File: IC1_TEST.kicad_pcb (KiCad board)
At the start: 4 copper layers, 26 parts, among them IC1 ADM3054WBRWZ-RL7-!my_lib, J1 B4B-XH-A_LF__SN_-!my_lib, SW1 SW_DIP_x03, SW2 SW_Push, U1 DEV-16771, U2 MAX6369KA+T

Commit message: wiring changes
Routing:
- net DIO_BUTTON: track 62.9 -> 58.9 mm
- net DIO_WATCHDOG: track 92.9 -> 89.5 mm
- net LED1: track 94.1 -> 97.0 mm
- net 3.3v_SUPPLY: track 246.1 -> 248.0 mm
- net SET2: track 18.3 -> 20.1 mm
- net SET1: track 37.8 -> 39.0 mm
- net LED2: track 70.0 -> 69.0 mm
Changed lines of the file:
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@@
     )
   )
-  (segment (start 195.633564 87.775489) (end 204.216 85.852) (width 0.25) (layer "F.Cu") (net 1))
-  (segment (start 206.756 116.84) (end 185.839295 135.89) (width 0.25) (layer "F.Cu") (net 1))
-  (segment (start 204.216 85.852) (end 206.756 85.852) (width 0.25) (layer "F.Cu") (net 1))
-  (segment (start 206.756 85.852) (end 206.756 116.84) (width 0.25) (layer "F.Cu") (net 1))
-  (segment (start 189.134052 94.275001) (end 195.633564 87.775489) (width 0.25) (layer "F.Cu") (net 1))
+  (segment (start 189.134052 94.275001) (end 195.58 87.376) (width 0.25) (layer "F.Cu") (net 1))
+  (segment (start 205.232 117.324273) (end 185.839295 135.89) (width 0.25) (layer "F.Cu") (net 1))
+  (segment (start 205.232 86.868) (end 205.232 117.324273) (width 0.25) (layer "F.Cu") (net 1))
   (segment (start 185.839295 135.89) (end 172.72 135.89) (width 0.25) (layer "F.Cu") (net 1))
+  (segment (start 195.58 87.376) (end 205.232 86.868) (width 0.25) (layer "F.Cu") (net 1))
   (segment (start 135.0137 142.875) (end 136.525 142.875) (width 0.25) (layer "F.Cu") (net 2))
   (segment (start 135.0137 149.225) (end 137.863402 149.225) (width 0.25) (layer "F.Cu") (net 2))
@@
   (segment (start 185.674 109.22) (end 185.674 96.266) (width 0.25) (layer "In1.Cu") (net 4))
   (segment (start 185.674 96.266) (end 185.928 96.012) (width 0.25) (layer "In1.Cu") (net 4))
-  (segment (start 191.865948 96.224999) (end 198.415001 96.224999) (width 0.25) (layer "F.Cu") (net 5))
-  (segment (start 198.415001 96.224999) (end 203.2 91.44) (width 0.25) (layer "F.Cu") (net 5))
+  (segment (start 203.2 91.44) (end 199.136 97.028) (width 0.25) (layer "F.Cu") (net 5))
+  (segment (start 199.136 97.028) (end 192.668949 97.028) (width 0.25) (layer "F.Cu") (net 5))
+  (segment (start 192.668949 97.028) (end 191.865948 96.224999) (width 0.25) (layer "F.Cu") (net 5))
   (segment (start 223.52 101.6) (end 217.894511 95.974511) (width 0.25) (layer "B.Cu") (net 5))
   (segment (start 205.74 91.44) (end 203.2 91.44) (width 0.25) (layer "B.Cu") (net 5))
   (segment (start 217.894511 95.974511) (end 210.274511 95.974511) (width 0.25) (layer "B.Cu") (net 5))
   (segment (start 210.274511 95.974511) (end 205.74 91.44) (width 0.25) (layer "B.Cu") (net 5))
+  (segment (start 195.072 96.52) (end 198.628 96.52) (width 0.25) (layer "F.Cu") (net 6))
   (segment (start 203.2 93.98) (end 203.2 100.33) (width 0.25) (layer "F.Cu") (net 6))
-  (segment (start 197.832948 95.575001) (end 198.882449 94.5255) (width 0.25) (layer "F.Cu") (net 6))
-  (segment (start 191.865948 95.575001) (end 197.832948 95.575001) (width 0.25) (layer "F.Cu") (net 6))
+  (segment (start 194.127001 95.575001) (end 191.865948 95.575001) (width 0.25) (layer "F.Cu") (net 6))
+  (segment (start 195.072 96.52) (end 194.127001 95.575001) (width 0.25) (layer "F.Cu") (net 6))
+  (segment (start 198.628 96.52) (end 198.882449 94.5255) (width 0.25) (layer "F.Cu") (net 6))
   (via (at 198.882449 94.5255) (size 0.8) (drill 0.4) (layers "F.Cu" "B.Cu") (net 6))
   (segment (start 198.882449 94.5255) (end 199.427949 93.98) (width 0.25) (layer "In2.Cu") (net 6))
@@
   (segment (start 196.85 94.850501) (end 196.2745 94.275001) (width 0.25) (layer "F.Cu") (net 8))
   (segment (start 118.872 147.828) (end 118.872 128.016) (width 0.25) (layer "F.Cu") (net 8))
-  (segment (start 190.5 96.234419) (end 189.969009 96.76541) (width 0.25) (layer "F.Cu") (net 8))
   (segment (start 140.938911 144.811089) (end 137.795 147.955) (width 0.25) (layer "F.Cu") (net 8))
   (segment (start 157.48 151.13) (end 151.161089 144.811089) (width 0.25) (layer "F.Cu") (net 8))
+  (segment (start 180.705 97.536) (end 177.95 93.4) (width 0.25) (layer "F.Cu") (net 8))
   (segment (start 142.12 93.4) (end 171.45 93.4) (width 0.25) (layer "F.Cu") (net 8))
   (segment (start 137.795 147.955) (end 135.0137 147.955) (width 0.25) (layer "F.Cu") (net 8))
-  (segment (start 191.865948 94.275001) (end 191.161374 94.275001) (width 0.25) (layer "F.Cu") (net 8))
   (segment (start 135.0137 147.955) (end 131.1247 147.955) (width 0.25) (layer "F.Cu") (net 8))
-  (segment (start 189.969009 96.76541) (end 181.31541 96.76541) (width 0.25) (layer "F.Cu") (net 8))
+  (segment (start 190.5 94.936375) (end 190.5 97.536) (width 0.25) (layer "F.Cu") (net 8))
   (segment (start 137.77 89.05) (end 142.12 93.4) (width 0.25) (layer "F.Cu") (net 8))
-  (segment (start 191.161374 94.275001) (end 190.5 94.936375) (width 0.25) (layer "F.Cu") (net 8))
   (segment (start 196.2745 94.275001) (end 191.865948 94.275001) (width 0.25) (layer "F.Cu") (net 8))
   (segment (start 151.161089 144.811089) (end 140.938911 144.811089) (width 0.25) (layer "F.Cu") (net 8))
+  (segment (start 190.5 97.536) (end 180.705 97.536) (width 0.25) (layer "F.Cu") (net 8))
+  (segment (start 191.865948 94.275001) (end 191.161374 94.275001) (width 0.25) (layer "F.Cu") (net 8))
   (segment (start 215.900001 158.75) (end 215.9 123.444) (width 0.25) (layer "F.Cu") (net 8))
-  (segment (start 181.31541 96.76541) (end 177.95 93.4) (width 0.25) (layer "F.Cu") (net 8))
-  (segment (start 190.5 94.936375) (end 190.5 96.234419) (width 0.25) (layer "F.Cu") (net 8))
+  (segment (start 191.161374 94.275001) (end 190.5 94.936375) (width 0.25) (layer "F.Cu") (net 8))
   (segment (start 215.9 123.444) (end 207.659011 95.25) (width 0.25) (layer "F.Cu") (net 8))
   (segment (start 118.872 128.016) (end 137.77 89.05) (width 0.25) (layer "F.Cu") (net 8))
@@
   (segment (start 161.036 159.512) (end 172.72 153.67) (width 0.25) (layer "B.Cu") (net 16))
   (segment (start 149.86 123.952) (end 149.86 159.512) (width 0.25) (layer "B.Cu") (net 16))
+  (segment (start 112.776 150.368) (end 112.776 169.164) (width 0.25) (layer "In1.Cu") (net 17))
+  (segment (start 112.92 139.7) (end 112.776 150.368) (width 0.25) (layer "In1.Cu") (net 17))
+  (segment (start 112.776 169.164) (end 154.94 169.164) (width 0.25) (layer "In1.Cu") (net 17))
   (segment (start 154.94 169.164) (end 172.72 151.13) (width 0.25) (layer "In1.Cu") (net 17))
-  (segment (start 115.824 169.164) (end 154.94 169.164) (width 0.25) (layer "In1.Cu") (net 17))
-  (segment (start 113.792 151.384) (end 115.824 169.164) (width 0.25) (layer "In1.Cu") (net 17))
-  (segment (start 112.92 139.7) (end 113.792 151.384) (width 0.25) (layer "In1.Cu") (net 17))
-  (segment (start 166.026696 148.59) (end 152.908 164.592) (width 0.25) (layer "In1.Cu") (net 18))
-  (segment (start 172.72 148.59) (end 166.026696 148.59) (width 0.25) (layer "In1.Cu") (net 18))
-  (segment (start 152.908 164.592) (end 137.16 164.592) (width 0.25) (layer "In1.Cu") (net 18))
+  (segment (start 172.72 148.59) (end 156.464 164.592) (width 0.25) (layer "In1.Cu") (net 18))
   (segment (start 137.16 164.592) (end 127 139.7) (width 0.25) (layer "In1.Cu") (net 18))
+  (segment (start 156.464 164.592) (end 137.16 164.592) (width 0.25) (layer "In1.Cu") (net 18))
   (segment (start 104.14 144.292493) (end 121.401753 166.116) (width 0.25) (layer "F.Cu") (net 19))
   (segment (start 104.14 139.7) (end 104.14 144.292493) (width 0.25) (layer "F.Cu") (net 19))
   (segment (start 152.654 166.116) (end 172.72 146.05) (width 0.25) (layer "F.Cu") (net 19))
   (segment (start 121.401753 166.116) (end 152.654 166.116) (width 0.25) (layer "F.Cu") (net 19))
-  (segment (start 185.42 154.94) (end 184.15 158.75) (width 0.25) (layer "B.Cu") (net 20))
-  (segment (start 172.72 143.51) (end 184.15 154.94) (width 0.25) (layer "B.Cu") (net 20))
-  (segment (start 220.600001 158.75) (end 220.472 154.94) (width 0.25) (layer "B.Cu") (net 20))
-  (segment (start 184.15 154.94) (end 184.15 158.75) (width 0.25) (layer "B.Cu") (net 20))
-  (segment (start 220.472 154.94) (end 185.42 154.94) (width 0.25) (layer "B.Cu") (net 20))
+  (segment (start 182.88 151.892) (end 174.498 143.51) (width 0.25) (layer "B.Cu") (net 20))
+  (segment (start 182.88 151.892) (end 182.88 156.972) (width 0.25) (layer "B.Cu") (net 20))
+  (segment (start 220.600001 158.75) (end 219.456 156.972) (width 0.25) (layer "B.Cu") (net 20))
+  (segment (start 174.498 143.51) (end 172.72 143.51) (width 0.25) (layer "B.Cu") (net 20))
+  (segment (start 186.436 156.972) (end 184.15 158.75) (width 0.25) (layer "B.Cu") (net 20))
+  (segment (start 182.88 156.972) (end 184.15 158.75) (width 0.25) (layer "B.Cu") (net 20))
+  (segment (start 219.456 156.972) (end 186.436 156.972) (width 0.25) (layer "B.Cu") (net 20))
   (segment (start 144.78 120.65) (end 157.48 120.65) (width 0.25) (layer "In1.Cu") (net 27))
   (segment (start 135.7249 146.685) (end 153.416 128.9939) (width 0.25) (layer "F.Cu") (net 30))

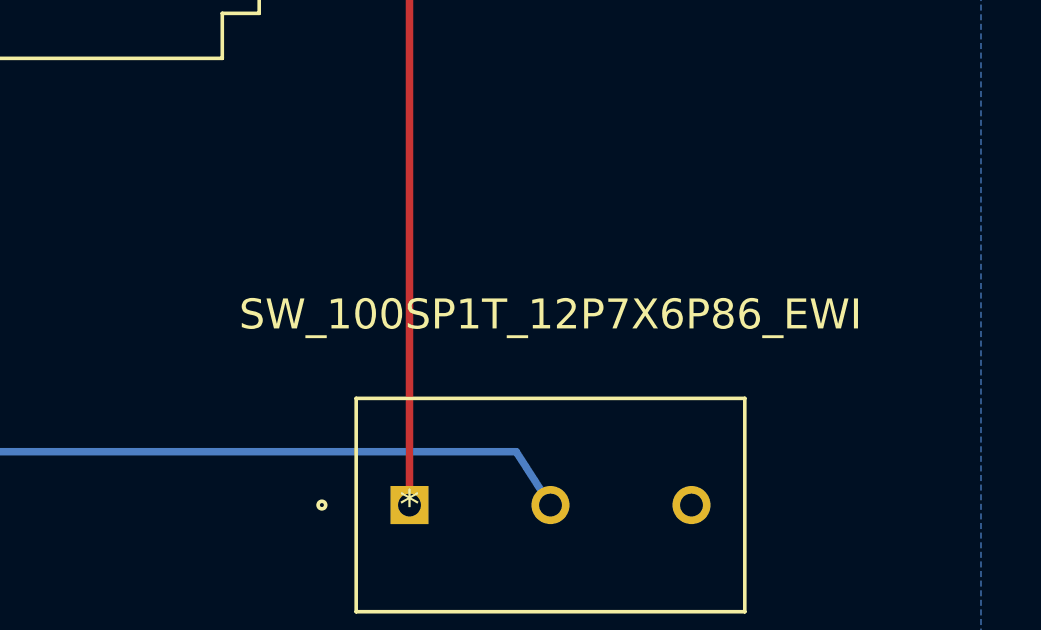
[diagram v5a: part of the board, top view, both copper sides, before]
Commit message: added watchdog output connection to teensy
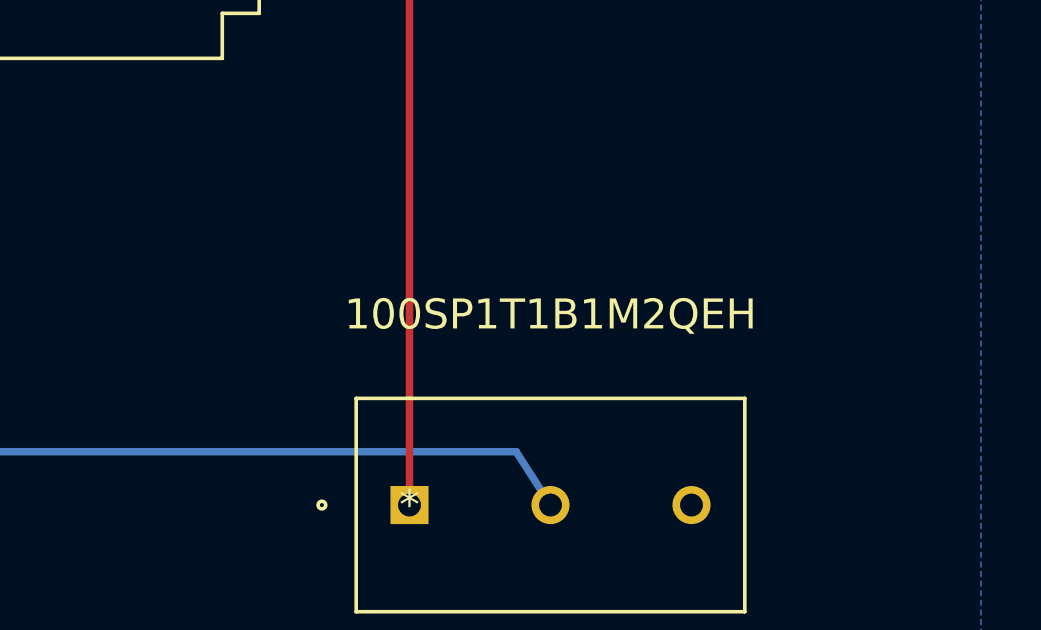
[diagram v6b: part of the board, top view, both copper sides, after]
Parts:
- reset_switch1: value SW_100SP1T_12P7X6P86_EWI -> 100SP1T1B1M2QEH
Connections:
- U1 pad 17: unconnected-(U1-Pad17) -> WATCHDOG_OUTPUT
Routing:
- net WATCHDOG_OUTPUT: track 26.4 -> 55.3 mm
